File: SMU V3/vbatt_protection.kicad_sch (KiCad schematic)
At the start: 5 parts, among them Q1 SI2301CDS-T1-GE3

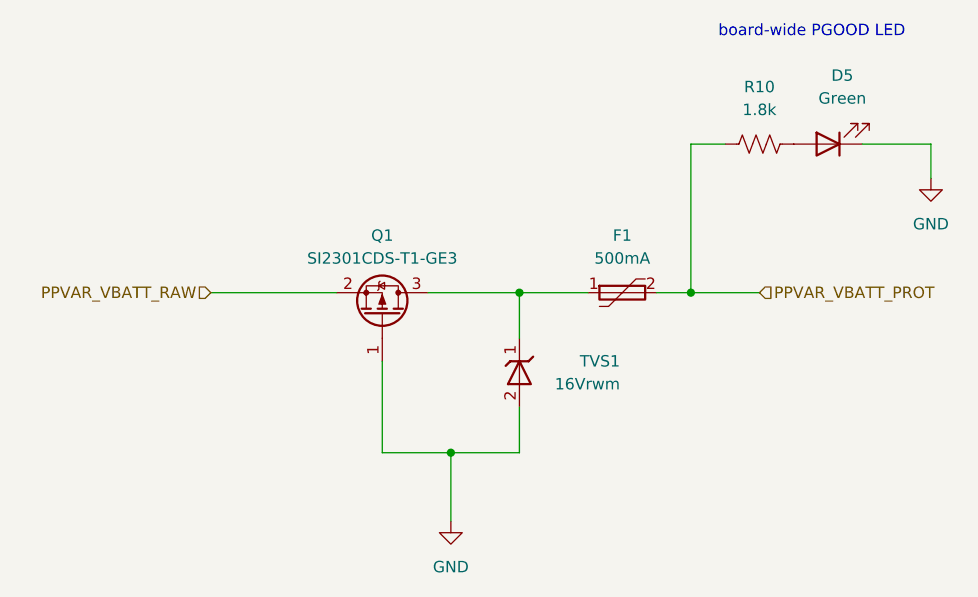
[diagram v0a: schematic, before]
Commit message: improved V3
added uart/spi test points and status leds
removed main 3v3 ldo
added silkscreen
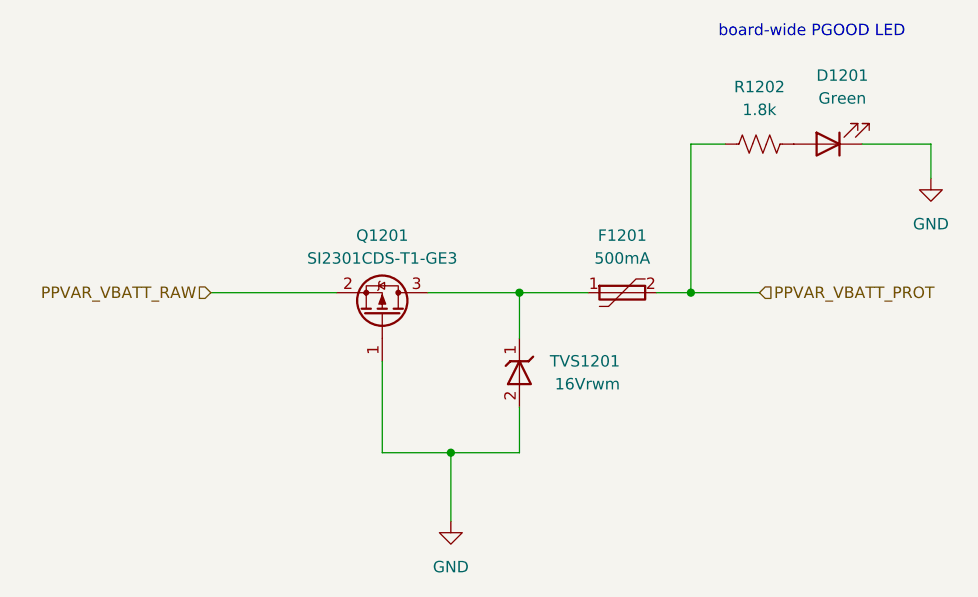
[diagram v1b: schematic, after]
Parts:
- renumbered D5 to D1201, F1 to F1201, Q1 to Q1201, R10 to R1202, TVS1 to TVS1201
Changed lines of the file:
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@@
 		(dnp no)
 		(fields_autoplaced yes)
-		(property "Reference" "F1"
+		(property "Reference" "F1201"
 			(at 152.4 81.28 0)
 			(show_name no)
@@
 			(project "SMU V3"
 				(path "/1f58b889-96e6-4877-90a3-5a655db5910b/b9f10619-4e5b-45af-b866-c6815d605ed5/ffadd9c2-fe2d-4025-92ac-e8757544fe06"
-					(reference "F1")
+					(reference "F1201")
 					(unit 1)
 				)
@@
 		(dnp no)
 		(fields_autoplaced yes)
-		(property "Reference" "#PWR037"
+		(property "Reference" "#PWR01201"
 			(at 186.69 81.28 0)
 			(hide yes)
@@
 			(project "SMU V3"
 				(path "/1f58b889-96e6-4877-90a3-5a655db5910b/b9f10619-4e5b-45af-b866-c6815d605ed5/ffadd9c2-fe2d-4025-92ac-e8757544fe06"
-					(reference "#PWR037")
+					(reference "#PWR01201")
 					(unit 1)
 				)
@@
 		(in_pos_files yes)
 		(dnp no)
-		(property "Reference" "TVS1"
+		(property "Reference" "TVS1201"
 			(at 152.146 95.25 90)
 			(show_name no)
@@
 			(project "SMU V3"
 				(path "/1f58b889-96e6-4877-90a3-5a655db5910b/b9f10619-4e5b-45af-b866-c6815d605ed5/ffadd9c2-fe2d-4025-92ac-e8757544fe06"
-					(reference "TVS1")
+					(reference "TVS1201")
 					(unit 1)
 				)
@@
 		(dnp no)
 		(fields_autoplaced yes)
-		(property "Reference" "D5"
+		(property "Reference" "D1201"
 			(at 176.8475 63.5 0)
 			(show_name no)
@@
 			(project "SMU V3"
 				(path "/1f58b889-96e6-4877-90a3-5a655db5910b/b9f10619-4e5b-45af-b866-c6815d605ed5/ffadd9c2-fe2d-4025-92ac-e8757544fe06"
-					(reference "D5")
+					(reference "D1201")
 					(unit 1)
 				)
@@
 		(dnp no)
 		(fields_autoplaced yes)
-		(property "Reference" "R10"
+		(property "Reference" "R1202"
 			(at 167.64 64.77 0)
 			(show_name no)
@@
 			(project "SMU V3"
 				(path "/1f58b889-96e6-4877-90a3-5a655db5910b/b9f10619-4e5b-45af-b866-c6815d605ed5/ffadd9c2-fe2d-4025-92ac-e8757544fe06"
-					(reference "R10")
+					(reference "R1202")
 					(unit 1)
 				)
@@
 		(dnp no)
 		(fields_autoplaced yes)
-		(property "Reference" "#PWR034"
+		(property "Reference" "#PWR01204"
 			(at 133.35 119.38 0)
 			(hide yes)
@@
 			(project "SMU V3"
 				(path "/1f58b889-96e6-4877-90a3-5a655db5910b/b9f10619-4e5b-45af-b866-c6815d605ed5/ffadd9c2-fe2d-4025-92ac-e8757544fe06"
-					(reference "#PWR034")
+					(reference "#PWR01204")
 					(unit 1)
 				)
@@
 		(in_pos_files yes)
 		(dnp no)
-		(property "Reference" "Q1"
+		(property "Reference" "Q1201"
 			(at 125.73 81.28 90)
 			(show_name no)
@@
 			(project "SMU V3"
 				(path "/1f58b889-96e6-4877-90a3-5a655db5910b/b9f10619-4e5b-45af-b866-c6815d605ed5/ffadd9c2-fe2d-4025-92ac-e8757544fe06"
-					(reference "Q1")
+					(reference "Q1201")
 					(unit 1)
 				)
